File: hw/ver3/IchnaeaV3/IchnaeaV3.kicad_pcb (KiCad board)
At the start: 4 copper layers, 100 x 100 mm, 330 parts, among them J1 Screw_Terminal_01x09, J2 Screw_Terminal_01x09, J3 Screw_Terminal_01x09, J4 Screw_Terminal_01x09, J5 FanConnector, Q1 BSS138, Q10 MCAC80N10Y, Q11 MCAC80N10Y, Q12 BSS138, Q13 BSS138, Q14 BSS138, Q15 BSS84, Q16 BSS138, Q17 MCAC80N10Y, Q18 MCAC80N10Y, Q2 MCAC80N10Y, Q3 MCAC80N10Y, Q4 MCAC80N10Y, Q5 MCAC80N10Y, Q6 MCAC80N10Y, Q7 MCAC80N10Y, Q8 MCAC80N10Y, Q9 MCAC80N10Y, U1 INA180A4, U10 HIP2210, U11 HIP2210, U16 ADS1220xPW, U17 74HC4051PW, U18 74HC4051PW, U2 LTC7871, U3 AP66200FVBW-13, U4 LM1117MP-5.0, U5 LM1117MP-3.3, U6 HIP2210, U7 HIP2210, U8 HIP2210, U9 HIP2210

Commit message: Tested the V2 board at 1.15kW load. Made some notes on system design for V3.
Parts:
- C29, C30, C36, C37, C51, C52, C55, C56, C57, C73, C74, C78, C79, C80, C81: moved to B.Cu
- moved H2 212.9 mm to (173.0, 115.0)
- moved H1 161.4 mm to (117.0, 115.0)
- moved C40 121.3 mm to (151.5, 101.5)
- moved C29 118.7 mm to (179.0, 94.5), turned to 180 degrees
- moved C30 118.1 mm to (179.0, 98.0), turned to 180 degrees
- moved C41 115.4 mm to (151.5, 98.0)
- moved C62 113.5 mm to (99.2, 94.5)
- moved H3 107.5 mm to (67.0, 112.5)
- moved C51 102.2 mm to (179.0, 101.5), turned to 180 degrees
- moved C52 99.6 mm to (151.5, 94.5), turned to 180 degrees
- moved C63 97.4 mm to (123.5, 94.5)
- moved C84 95.9 mm to (99.2, 98.0)
- moved C85 95.2 mm to (99.2, 101.5)
- moved C74 82.1 mm to (123.5, 101.5)
- moved C73 74.3 mm to (123.5, 98.0)
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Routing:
- net VLOW: vias 0 -> 48
- net VHIGH: vias 0 -> 27
- added copper zone on In1.Cu, net GND
- added copper zone on In2.Cu, net GND
- added copper zone on F.Cu, net VLOW

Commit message: Cost optimize power terminal connections
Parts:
- removed C93: 100nF, Capacitor_SMD:C_0603_1608Metric
- removed J3, J4: Screw_Terminal_01x09, Connectors:CONN_74651195R_WRE
- removed L1: 1.5mH, Inductor_SMD:L_Changjiang_FNR6045S
- removed R75: 100k, Resistor_SMD:R_0603_1608Metric
- removed TP1, TP16, TP17, TP19, TP2, TP20, TP21, TP3, TP60, TP61: TestPoint, TestPoint:TestPoint_Pad_D1.0mm
- added C101: 100nF, Capacitor_SMD:C_0603_1608Metric, B.Cu at (162.3, 58.0)
- added C102: 100nF, Capacitor_SMD:C_0603_1608Metric, B.Cu at (162.3, 60.5)
- added C103: 100nF, Capacitor_SMD:C_0603_1608Metric, B.Cu at (130.3, 65.0)
- added C104: 100nF, Capacitor_SMD:C_0603_1608Metric, B.Cu at (130.0, 67.0)
- added C105: 100nF, Capacitor_SMD:C_0603_1608Metric, B.Cu at (162.3, 62.5)
- added R95: 0.2m, Resistors:Shunt_5930, F.Cu at (136.0, 65.5)
- added R96: 5.1k, Resistor_SMD:R_0603_1608Metric, B.Cu at (162.3, 65.0)
- added R97: 10k, Resistor_SMD:R_0603_1608Metric, B.Cu at (162.3, 67.5)
- added U19: INA180A4, Package_TO_SOT_SMD:SOT-23-5, B.Cu at (156.8, 61.8)
- C1, D1, D2, R2, R3, R4, R5, U1: moved to B.Cu
- GD1, GD2: value 90V-2kA -> GDT_2Pin; moved to B.Cu
- J1, J2: value Screw_Terminal_01x09 -> Terminal Block; footprint Connectors:CONN_74651195R_WRE -> Connectors:KF88SA-16.0-2P
- R12: value 470k -> 348k; footprint Resistor_SMD:R_0805_2012Metric -> Resistor_SMD:R_0603_1608Metric
- R13: value 15k -> 12k
- moved U1 157.6 mm to (126.5, 65.0), turned to 180 degrees
- moved C1 153.3 mm to (130.2, 58.0), turned to 180 degrees
- moved R4 153.3 mm to (130.2, 60.5), turned to 180 degrees
- moved R5 153.3 mm to (130.2, 63.0), turned to 180 degrees
- moved H3 93.7 mm to (145.0, 60.5)
- moved GD2 65.6 mm to (113.0, 70.0)
- moved GD1 65.1 mm to (177.0, 70.0), turned to 0 degrees
- moved J1 17.4 mm to (113.0, 65.5)
- moved H1 16.0 mm to (117.0, 131.0)
- moved H2 16.0 mm to (173.0, 131.0)
- moved J2 10.3 mm to (177.0, 65.5), turned to 180 degrees
- moved R1 9.66 mm to (154.0, 65.5), turned to -90 degrees
- moved C29 7.00 mm to (179.0, 101.5)
- moved C30 7.00 mm to (179.0, 105.0)
- moved C33 7.00 mm to (108.0, 107.5)
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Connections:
- net /CTL_IN_ADC_IBATT_SENSE renamed ISENSE_OUTPUT
- C11 pad 1: Net-(U4-VI) -> +12V
- C12 pad 1: Net-(U4-VI) -> +12V
- C13 pad 1: Net-(U4-VI) -> +12V
- C29 pad 1: VHIGH -> VIN
- C30 pad 1: VHIGH -> VIN
- C40 pad 1: VHIGH -> VIN
- C41 pad 1: VHIGH -> VIN
- C51 pad 1: VHIGH -> VIN
- C52 pad 1: VHIGH -> VIN
- C62 pad 1: VHIGH -> VIN
- C63 pad 1: VHIGH -> VIN
- C73 pad 1: VHIGH -> VIN
- C74 pad 1: VHIGH -> VIN
- C84 pad 1: VHIGH -> VIN
- C85 pad 1: VHIGH -> VIN
- D1 pad 1: VHIGH -> VIN
- D1 pad 2: GND -> /InputGND
- D2 pad 1: VLOW -> VOUT
- D2 pad 2: GNDBATT -> /OutputGND
- GD1 pad 1: GND -> /OutputGND
- GD1 pad 2: VHIGH -> VOUT
- GD2 pad 1: GNDBATT -> VIN
- GD2 pad 2: VLOW -> /InputGND
- J1 pad 1: VHIGH -> VIN
- J1 pad 2: VHIGH -> /InputGND
- J2 pad 1: VLOW -> VOUT
- J2 pad 2: VLOW -> /OutputGND
- Q10 pad 1: VHIGH -> VIN
- Q17 pad 1: VHIGH -> VIN
- Q2 pad 1: VHIGH -> VIN
- Q4 pad 1: VHIGH -> VIN
- Q6 pad 1: VHIGH -> VIN
- Q8 pad 1: VHIGH -> VIN
- R1 pad 1: GND -> /OutputGND
- R1 pad 2: GNDBATT -> GND
- R18 pad 1: VHIGH -> VIN
- R2 pad 1: VHIGH -> VIN
- R2 pad 2: GND -> /InputGND
- R3 pad 1: VLOW -> VOUT
- R3 pad 2: GNDBATT -> /OutputGND
- R8 pad 1: VHIGH -> VIN
- R9 pad 1: VHIGH -> VIN
- U1 pad 3: GNDBATT -> GND
- U1 pad 4: GND -> /OutputGND
- U2 pad 10: /PowerStage/IO_LTC_IMON -> unconnected-(U2-IMON-Pad10)
- U2 pad 48: VHIGH -> VIN
- U4 pad 3: Net-(U4-VI) -> +12V
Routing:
- net VIN: vias 0 -> 27
- net VHIGH: vias 27 -> 0
- net GND: vias 0 -> 76
- added copper zone on F.Cu, net /InputGND
- added copper zone on F.Cu, net /OutputGND
- added copper zone on F.Cu, net GND

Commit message: Improve more of the power stage layout
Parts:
- removed C100, C99: 100nF, Capacitor_SMD:C_0603_1608Metric
- removed C21, C23, C24: 10uF-25V, Capacitor_SMD:C_0603_1608Metric
- removed D4: ESD9B3.3ST5G, Diode_SMD:D_SOD-923
- removed R5, R60, R61, R65, R67, R91, R92, R97: 10k, Resistor_SMD:R_0603_1608Metric
- removed R58, R59, R63, R64: 100, Resistor_SMD:R_0603_1608Metric
- removed R93, R94: 100k, Resistor_SMD:R_0603_1608Metric
- removed TP24, TP25, TP26, TP27, TP28, TP30, TP31, TP32, TP33, TP34, TP36, TP37, TP38, TP39, TP40, TP42, TP43, TP44, TP45, TP46, TP48, TP49, TP50, TP51, TP52, TP54, TP55, TP56, TP57, TP58, TP71, TP72: TestPoint, TestPoint:TestPoint_Pad_D1.0mm
- removed U5: LM1117MP-3.3, Package_TO_SOT_SMD:SOT-223-3_TabPin2
- added C106: 1uF, Capacitor_SMD:C_0603_1608Metric, F.Cu at (193.0, 98.2)
- added C107: 1uF, Capacitor_SMD:C_0603_1608Metric, F.Cu at (192.5, 113.0)
- added C93: 1uF, Capacitor_SMD:C_0603_1608Metric, F.Cu at (190.0, 98.2)
- added Q20: HYG053N10NS1C2, Mosfets:TRANS_BSC076N06NS3-G, B.Cu at (190.8, 83.2)
- added Q21: HYG053N10NS1C2, Mosfets:TRANS_BSC076N06NS3-G, B.Cu at (183.7, 77.2)
- added Q22: HYG053N10NS1C2, Mosfets:TRANS_BSC076N06NS3-G, B.Cu at (190.8, 77.3)
- added Q23: HYG053N10NS1C2, Mosfets:TRANS_BSC076N06NS3-G, B.Cu at (183.7, 83.2)
- added Q24: HYG053N10NS1C2, Mosfets:TRANS_BSC076N06NS3-G, B.Cu at (190.8, 94.8)
- added Q25: HYG053N10NS1C2, Mosfets:TRANS_BSC076N06NS3-G, B.Cu at (183.7, 89.0)
- added Q26: HYG053N10NS1C2, Mosfets:TRANS_BSC076N06NS3-G, B.Cu at (190.8, 89.0)
- added Q27: HYG053N10NS1C2, Mosfets:TRANS_BSC076N06NS3-G, B.Cu at (183.7, 94.8)
- added R75: 16.5k, Resistor_SMD:R_0603_1608Metric, F.Cu at (190.5, 119.8)
- added R98: 10k, Resistor_SMD:R_0603_1608Metric, F.Cu at (189.0, 119.8)
- added U20: TPSI3050, Package_SO:SOIC-8_7.5x5.85mm_P1.27mm, F.Cu at (191.2, 105.5)
- Q10, Q11, Q17, Q18, Q2, Q3, Q4, Q5, Q6, Q7, Q8, Q9: value MCAC80N10Y -> HYG053N10NS1C2
- R52: moved to B.Cu
- moved C75 117.9 mm to (132.2, 123.2)
- moved C76 117.9 mm to (132.2, 125.7)
- moved TP53 117.9 mm to (128.2, 151.8)
- moved R53 117.9 mm to (123.5, 154.9)
- moved R54 117.9 mm to (132.2, 135.7)
- moved C71 115.3 mm to (122.0, 125.2), turned to 180 degrees
- moved C72 106.4 mm to (125.0, 119.0), turned to 90 degrees
- moved R50 105.7 mm to (125.5, 125.8)
- moved R51 105.4 mm to (126.0, 128.0), turned to 180 degrees
- moved R52 97.5 mm to (121.2, 122.5)
- moved U10 88.6 mm to (121.8, 119.0), turned to 180 degrees
- moved C33 49.6 mm to (157.6, 107.5)
- moved C90 47.9 mm to (146.8, 73.5), turned to 90 degrees
- moved C59 36.3 mm to (129.6, 107.5), turned to -90 degrees
- moved C102 33.2 mm to (129.5, 65.5), turned to 90 degrees
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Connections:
- Q12 pad 1: Net-(Q12-G) -> LTC_RUN
- Q13 pad 1: Net-(Q13-G) -> LTC_SYNC
- Q14 pad 1: Net-(Q14-G) -> LTC_DCM
- Q16 pad 1: Net-(Q16-G) -> LTC_CCM
- R18 pad 1: VIN -> HT
- R57 pad 2: +3.3V -> +5V
- R76 pad 1: +3.3V -> +5V
- R8 pad 1: VIN -> HT
- R84 pad 2: VHIGH -> VIN
- R9 pad 1: VIN -> HT
- U1 pad 3: GND -> /OutputGND
- U1 pad 4: /OutputGND -> GND
- U19 pad 3: GND -> /InputGND
- U19 pad 4: /InputGND -> GND
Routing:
- net ISENSE_OUTPUT: track 0.00 -> 100.3 mm, vias 0 -> 1
- net ISENSE_INPUT: track 0.00 -> 82.7 mm, vias 0 -> 1
- net GND: track 0.00 -> 77.8 mm, vias 76 -> 125
- net VLOW: track 0.00 -> 21.0 mm, vias 48 -> 96
- net Net-(Q20-S): track 0.00 -> 8.43 mm, vias 0 -> 3
- net VIN: track 0.00 -> 7.00 mm
- net Net-(Q20-G): track 0.00 -> 6.96 mm, vias 0 -> 2
- net Net-(Q11-G): track 0.00 -> 5.96 mm
- net Net-(Q10-G): track 0.00 -> 5.10 mm
- net Net-(Q10-S): track 0.00 -> 4.31 mm
- net /OutputGND: track 0.00 -> 4.04 mm, vias 0 -> 24
- net /InputGND: track 0.00 -> 4.04 mm, vias 0 -> 24
- net Net-(R4-Pad2): track 0.00 -> 3.62 mm
- net Net-(U20-VDDM): track 0.00 -> 3.52 mm
- net Net-(R96-Pad2): track 0.00 -> 3.50 mm
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- added copper zone on In2.Cu, net +5V
- added copper zone on B.Cu, net /InputGND
- added copper zone on In1.Cu, net /InputGND
- added copper zone on In2.Cu, net /InputGND
- added copper zone on B.Cu, net /OutputGND
- added copper zone on In1.Cu, net /OutputGND
- added copper zone on In2.Cu, net /OutputGND
- added copper zone on B.Cu, net GND
- added copper zone on F.Cu, net Net-(Q10-S)
- added copper zone on B.Cu, net Net-(Q17-S)
- added copper zone on F.Cu, net Net-(Q2-S)
- added copper zone on B.Cu, net Net-(Q20-S)
- added copper zone on B.Cu, net Net-(Q4-S)
- added copper zone on F.Cu, net Net-(Q6-S)
- added copper zone on B.Cu, net Net-(Q8-S)
- added copper zone on B.Cu, net VIN
- added copper zone on B.Cu, net VLOW
- added copper zone on B.Cu, net VOUT
- removed copper zone on B.Cu, net VHIGH

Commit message: Start rework of power stage layout to shorten inductive path and increase current handling
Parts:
- removed TP29, TP35, TP41, TP47, TP53, TP59: TestPoint, TestPoint:TestPoint_Pad_D1.0mm
- C40, C62, C84, C85: moved to F.Cu
- moved C27 143.5 mm to (177.0, 122.8), turned to 180 degrees
- moved C31 138.6 mm to (183.2, 126.0), turned to 180 degrees
- moved C32 137.7 mm to (183.3, 127.6)
- moved C28 136.8 mm to (180.8, 119.8), turned to 90 degrees
- moved R31 135.1 mm to (174.0, 122.8), turned to 180 degrees
- moved R30 133.5 mm to (180.0, 122.8)
- moved R32 130.8 mm to (174.0, 119.8), turned to 90 degrees
- moved R34 130.8 mm to (183.3, 129.2)
- moved C49 128.4 mm to (150.0, 123.0)
- moved C53 126.3 mm to (150.3, 125.8)
- moved C42 125.9 mm to (162.5, 130.5)
- moved C54 125.3 mm to (150.3, 127.2)
- moved U6 123.0 mm to (177.2, 119.8), turned to 180 degrees
- moved C38 122.5 mm to (164.5, 122.8), turned to 0 degrees
- moved C43 122.4 mm to (162.5, 129.0)
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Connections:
- R22 pad 2: +3.3V -> +5V
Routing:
- net VLOW: track 21.0 -> 153.0 mm
- net GND: track 77.8 -> 25.2 mm, vias 125 -> 106
- net Net-(Q6-S): track 0.00 -> 29.2 mm, vias 0 -> 1
- net Net-(Q8-S): track 0.00 -> 29.0 mm, vias 0 -> 1
- net Net-(Q2-S): track 0.00 -> 27.5 mm, vias 0 -> 1
- net Net-(Q4-S): track 0.00 -> 27.1 mm, vias 0 -> 1
- net Net-(Q17-S): track 0.00 -> 23.2 mm, vias 0 -> 1
- net Net-(Q10-S): track 4.31 -> 25.6 mm, vias 0 -> 1
- net ISENSE_OUTPUT: track 100.3 -> 107.6 mm
- net VIN: track 7.00 -> 0.00 mm
- net ISENSE_INPUT: track 82.7 -> 89.6 mm
- net Net-(Q11-G): track 5.96 -> 0.00 mm
- net Net-(Q10-G): track 5.10 -> 0.00 mm
- net Net-(U10-HB): track 1.36 -> 0.00 mm
- removed copper zone on B.Cu, net GND

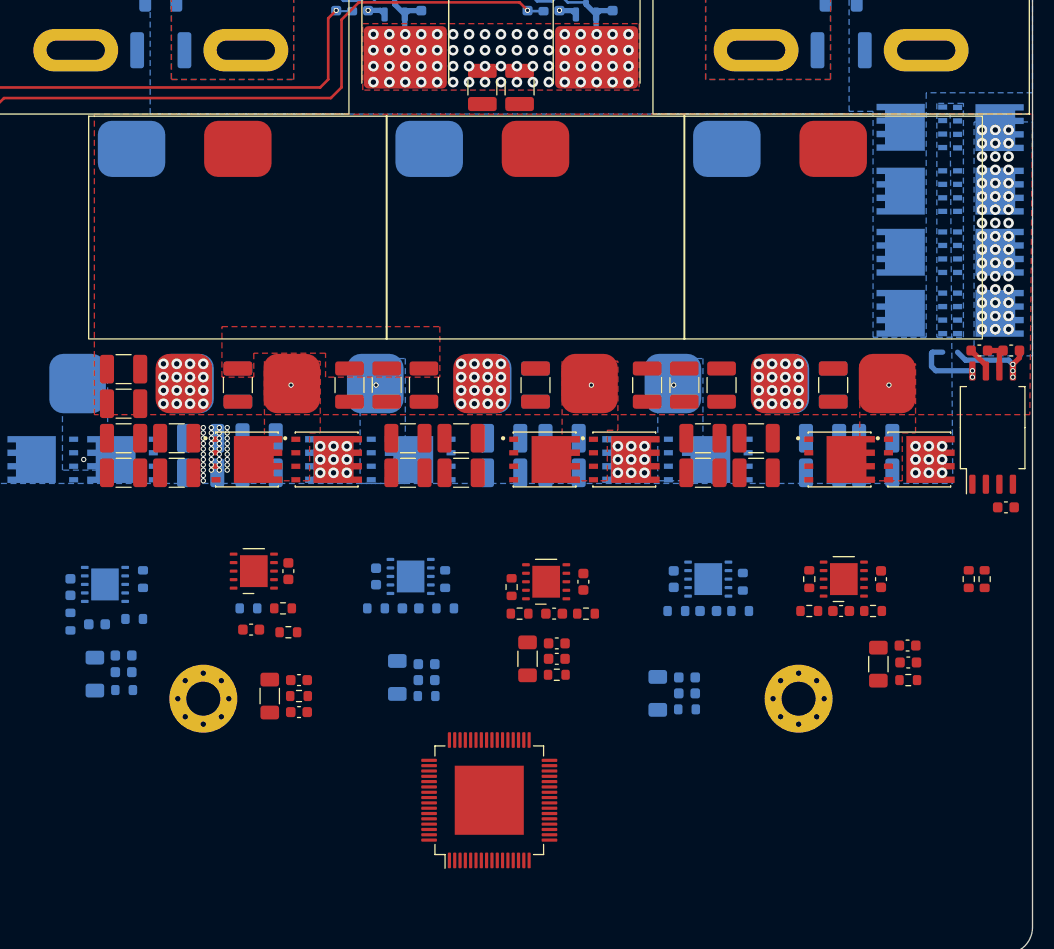
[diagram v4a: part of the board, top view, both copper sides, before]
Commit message: Greatly improve power routing. Add gate control drive.
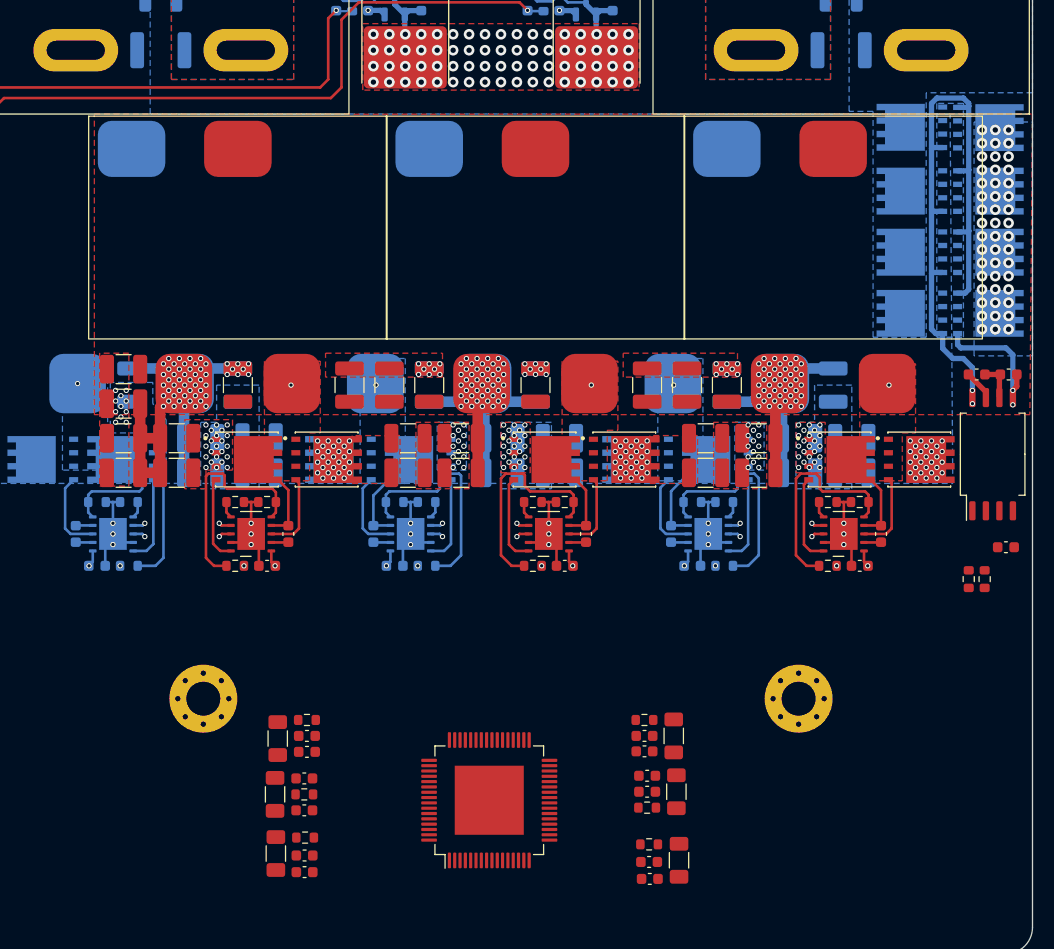
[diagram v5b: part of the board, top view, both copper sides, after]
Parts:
- C42, C43, C64, C65, C86, C87, R38, R39, R48, R49, R52, R72, R73: moved to F.Cu
- C45, C77, C90: moved to B.Cu
- moved C45 66.0 mm to (110.2, 101.5), turned to -90 degrees
- moved C90 34.1 mm to (166.2, 101.5)
- moved C31 32.7 mm to (159.0, 147.9), turned to 0 degrees
- moved C32 30.8 mm to (158.9, 146.4), turned to 180 degrees
- moved R34 28.9 mm to (158.9, 144.7), turned to 180 degrees
- moved C77 28.4 mm to (138.2, 101.5)
- moved C86 26.6 mm to (126.5, 147.3)
- moved R33 26.3 mm to (161.8, 146.2), turned to -90 degrees
- moved C87 24.2 mm to (126.5, 145.8)
- moved R72 24.0 mm to (123.8, 145.6), turned to -90 degrees
- moved R73 22.0 mm to (126.6, 144.1)
- moved R43 15.5 mm to (161.3, 134.5), turned to -90 degrees
- moved C64 14.0 mm to (126.8, 136.0)
- moved C53 13.1 mm to (158.5, 136.0), turned to 180 degrees
- moved R48 12.6 mm to (124.0, 134.8), turned to 90 degrees
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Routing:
- net VLOW: track 153.0 -> 226.3 mm, vias 96 -> 183
- net GND: track 25.2 -> 78.5 mm, vias 106 -> 226
- net Net-(Q20-G): track 6.96 -> 60.0 mm
- net /PowerStage/Phase1/PWMEN: track 0.00 -> 52.6 mm, vias 0 -> 6
- net Net-(U11-VREF): track 0.00 -> 21.4 mm
- net Net-(U9-VREF): track 0.00 -> 21.3 mm
- net Net-(U7-VREF): track 0.00 -> 21.0 mm
- net Net-(U6-VREF): track 0.00 -> 20.5 mm
- net Net-(U8-VREF): track 0.00 -> 20.5 mm
- net Net-(U10-VREF): track 0.00 -> 20.4 mm
- net /PowerStage/Phase6/PWM: track 0.00 -> 11.9 mm, vias 0 -> 1
- net /PowerStage/Phase5/PWM: track 0.00 -> 11.4 mm, vias 0 -> 1
- net /PowerStage/Phase4/PWM: track 0.00 -> 10.7 mm, vias 0 -> 1
- net /PowerStage/Phase2/PWM: track 0.00 -> 10.4 mm, vias 0 -> 1
- net /PowerStage/Phase3/PWM: track 0.00 -> 9.91 mm, vias 0 -> 1
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- added copper zone on B.Cu, net GND
- added copper zone on F.Cu, net VIN
